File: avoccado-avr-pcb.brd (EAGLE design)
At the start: 17.8 x 40.3 mm, 30 parts, among them IC1 MCP1703CB, IC5 ATMEGA328P-20MU, Q1 #MHz, Q2 MOSFET-NCHANNEL2N7002PW, U1 ATMEGA328P, U2 MCP73831, X1 Micro USB

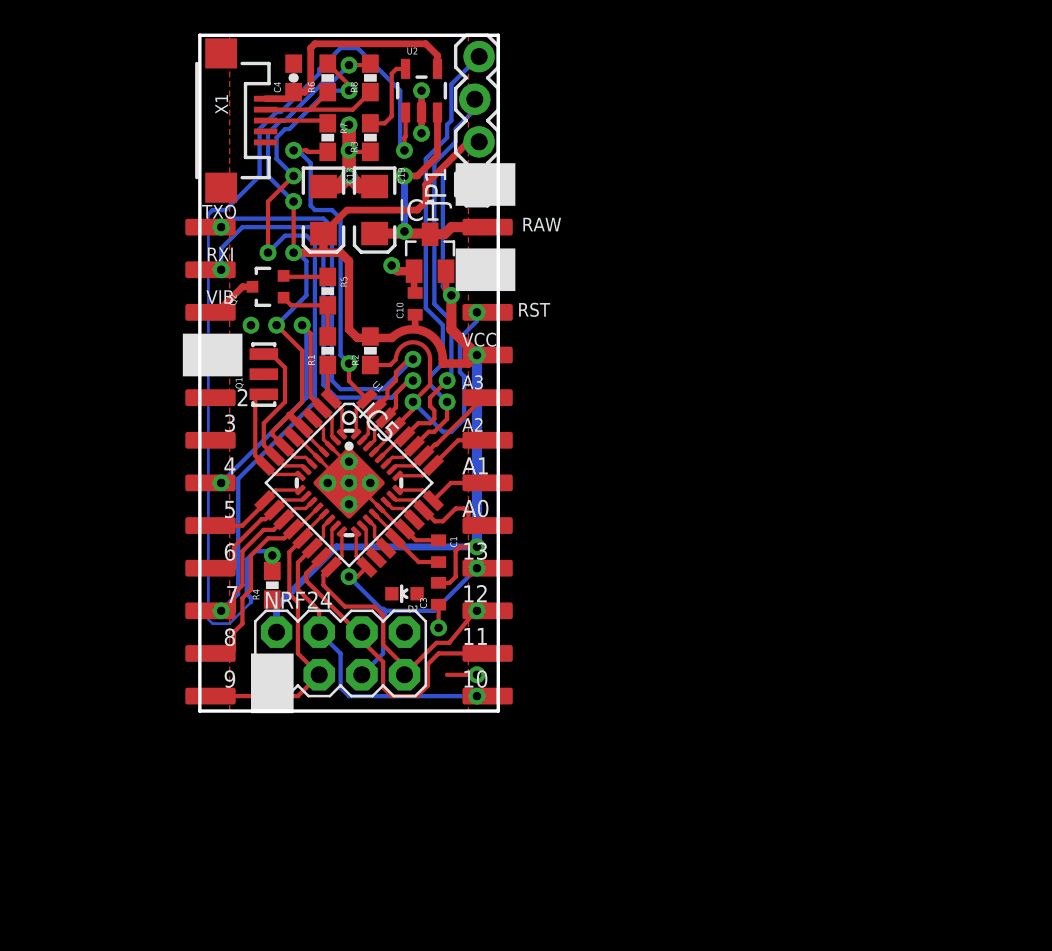
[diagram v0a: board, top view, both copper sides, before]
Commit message: reroute bottom header, reduce airwires
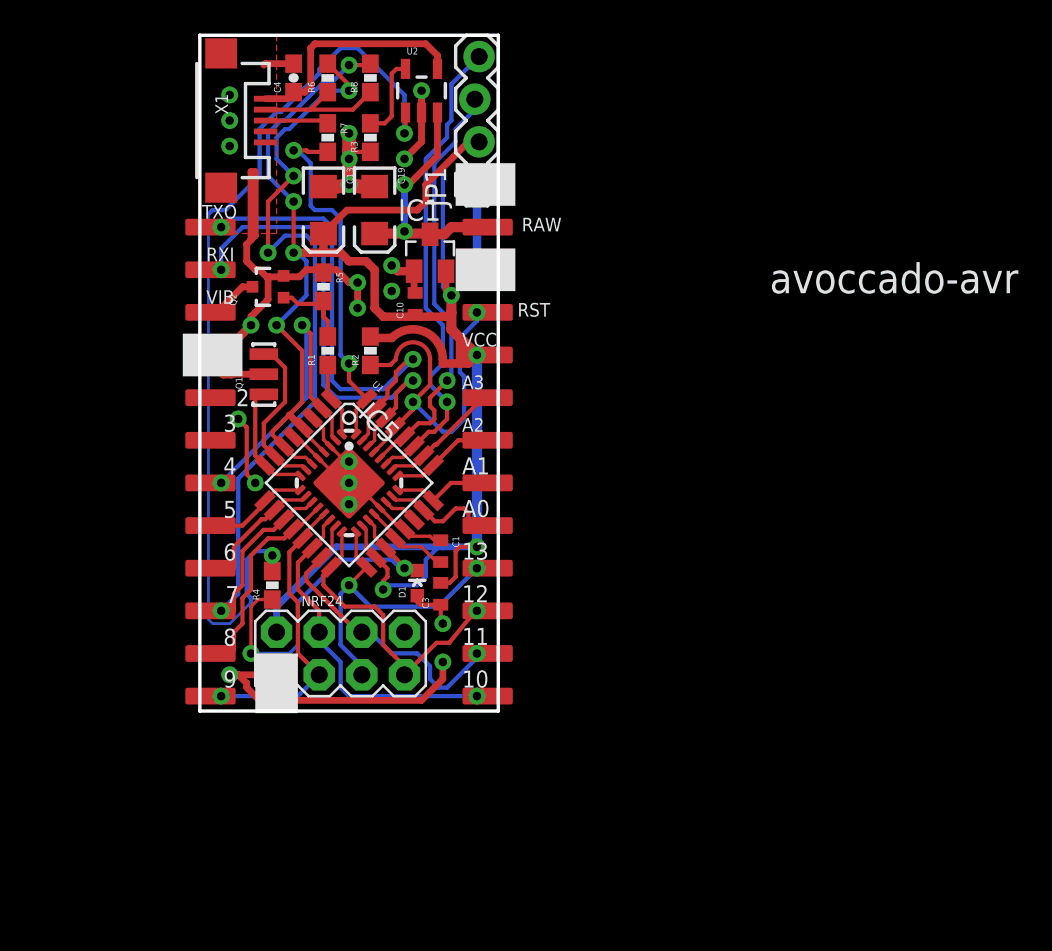
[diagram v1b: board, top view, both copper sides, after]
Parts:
- moved D1 0.99 mm to (21.8, 19.4), turned to 0 degrees
- moved R5 0.36 mm to (16.3, 37.1)
- moved C1 0.13 mm to (23.2, 21.3)
- moved C3 0.13 mm to (23.2, 18.8)
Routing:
- net GND: track 35.4 -> 99.2 mm, vias 16 -> 23
- net A6: track 2.13 -> 21.9 mm, vias 0 -> 2
- net 3V3: track 117.0 -> 127.6 mm, vias 7 -> 8
- net N$4: track 57.0 -> 55.0 mm
- net MOSI: track 20.7 -> 18.9 mm, vias 0 -> 1
- net SCK: track 18.2 -> 19.7 mm
- net BAT: track 16.9 -> 18.2 mm
- net D9: vias 0 -> 1

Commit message: minor corrections
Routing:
- net GND: track 99.2 -> 100.7 mm
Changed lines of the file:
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@@
 <layer number="14" name="Route14" color="1" fill="6" visible="no" active="no"/>
 <layer number="15" name="Route15" color="4" fill="6" visible="no" active="no"/>
-<layer number="16" name="Bottom" color="1" fill="1" visible="no" active="yes"/>
+<layer number="16" name="Bottom" color="1" fill="1" visible="yes" active="yes"/>
 <layer number="17" name="Pads" color="14" fill="1" visible="yes" active="yes"/>
 <layer number="18" name="Vias" color="14" fill="1" visible="yes" active="yes"/>
@@
 </layers>
 <board>
+<description>Avoccado-avr controller</description>
 <plain>
 <wire x1="8.89" y1="52.07" x2="8.89" y2="11.811" width="0.2032" layer="20"/>
@@
 <wire x1="17.78" y1="37.338" x2="17.018" y2="38.1" width="0.4064" layer="1"/>
 <wire x1="17.018" y1="38.1" x2="16.09" y2="38.1" width="0.4064" layer="1"/>
-<wire x1="18.288" y1="37.338" x2="18.288" y2="35.814" width="0.4064" layer="1"/>
 <via x="18.288" y="35.814" extent="1-16" drill="0.508" diameter="1.016"/>
 <via x="10.668" y="13.97" extent="1-16" drill="0.508" diameter="1.016"/>
@@
 <via x="11.176" y="29.21" extent="1-16" drill="0.508" diameter="1.016"/>
 <wire x1="11.684" y1="28.702" x2="11.176" y2="29.21" width="0.254" layer="1"/>
+<wire x1="20.32" y1="36.83" x2="20.32" y2="38.354" width="0.508" layer="1"/>
 <wire x1="10.16" y1="33.02" x2="9.525" y2="33.02" width="0" layer="19" extent="1-1"/>
 <wire x1="25.4" y1="38.1" x2="21.656" y2="38.016" width="0" layer="19" extent="1-1"/>
+<wire x1="18.288" y1="35.814" x2="18.288" y2="37.338" width="0.508" layer="1"/>
+<wire x1="18.288" y1="37.338" x2="25.4" y2="38.1" width="0" layer="19" extent="1-16"/>
 </signal>
 <signal name="AREF">
@@
 <contactref element="U1" pad="29"/>
 <contactref element="JP3" pad="3"/>
-<wire x1="26.035" y1="35.56" x2="25.4" y2="35.56" width="0.254" layer="1"/>
-<via x="25.4" y="35.56" extent="1-16" drill="0.508" diameter="1.016"/>
+<wire x1="26.035" y1="35.56" x2="25.019" y2="35.56" width="0.254" layer="1"/>
+<via x="25.019" y="35.56" extent="1-16" drill="0.508" diameter="1.016"/>
 <wire x1="23.368" y1="28.448" x2="23.876" y2="28.448" width="0.254" layer="16"/>
 <wire x1="23.876" y1="28.448" x2="24.638" y2="29.21" width="0.254" layer="16"/>
 <wire x1="24.638" y1="29.21" x2="24.638" y2="31.75" width="0.254" layer="16"/>
 <wire x1="24.638" y1="31.75" x2="24.384" y2="32.004" width="0.254" layer="16"/>
-<wire x1="24.384" y1="32.004" x2="24.384" y2="34.036" width="0.254" layer="16"/>
-<wire x1="24.384" y1="34.036" x2="25.4" y2="35.052" width="0.254" layer="16"/>
-<wire x1="25.4" y1="35.052" x2="25.4" y2="35.56" width="0.254" layer="16"/>
+<wire x1="24.384" y1="32.004" x2="24.384" y2="35.052" width="0.254" layer="16"/>
+<wire x1="24.384" y1="35.052" x2="25.019" y2="35.56" width="0.254" layer="16"/>
 <wire x1="20.53248125" y1="28.71816875" x2="21.59" y2="29.7756875" width="0.254" layer="1"/>
 <wire x1="21.59" y1="29.7756875" x2="21.59" y2="30.226" width="0.254" layer="1"/>

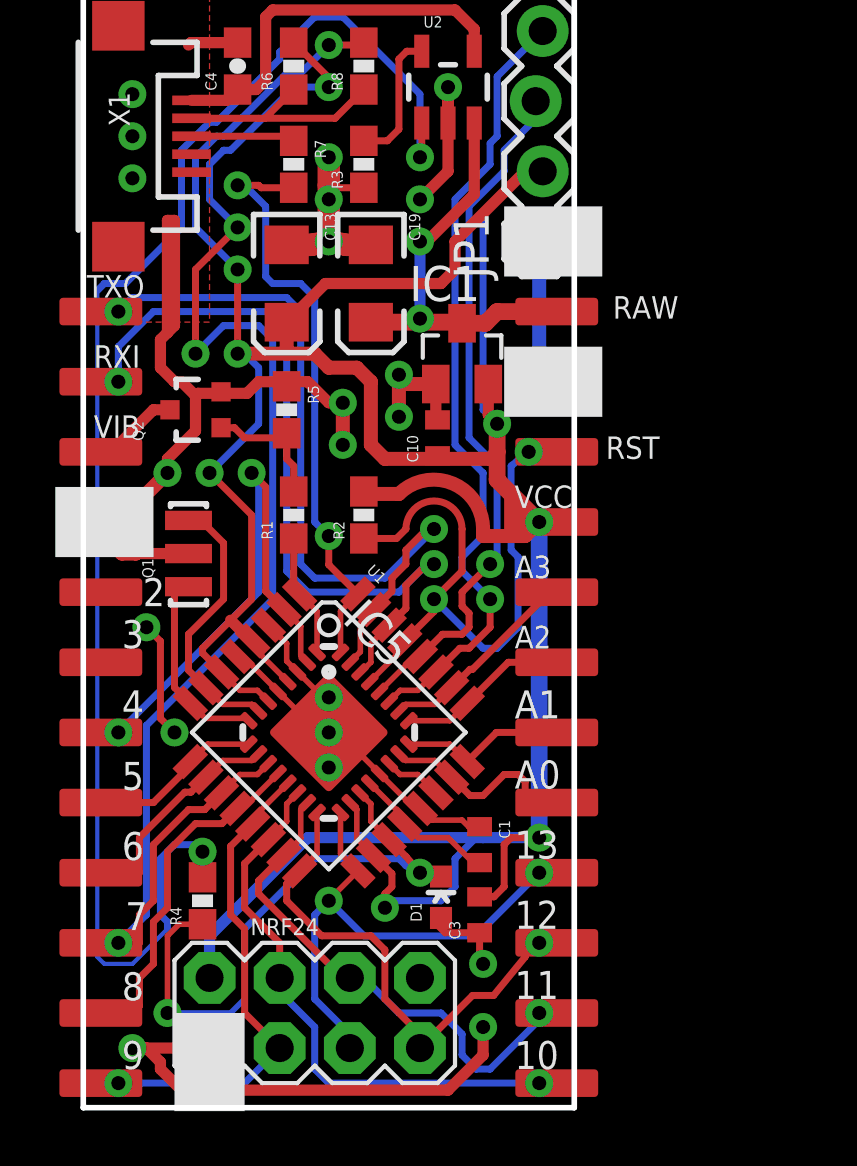
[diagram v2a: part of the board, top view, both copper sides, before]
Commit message: reroute GND layer, ditch pins 2&3
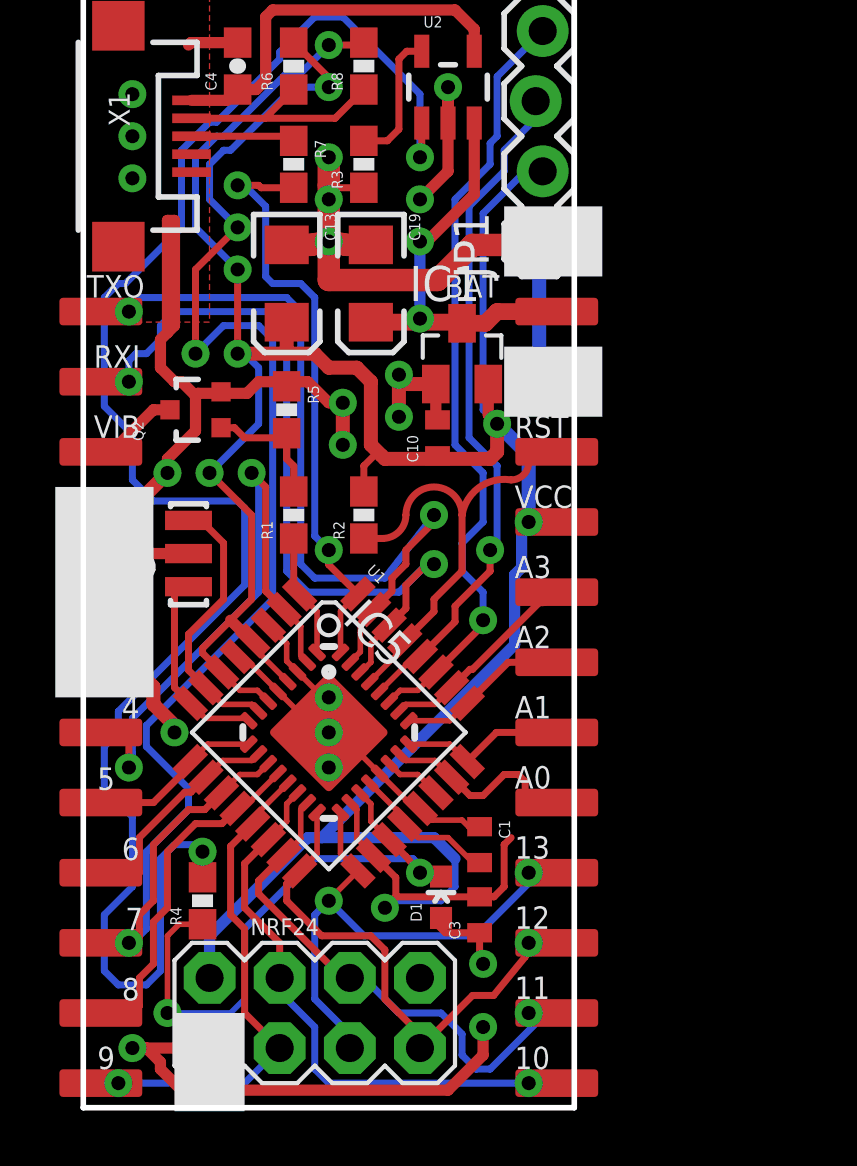
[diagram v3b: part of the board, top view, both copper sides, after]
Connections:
- net D2: no longer JP10.4
- net D3: no longer JP10.3
- net GND: now also JP10.3, JP10.4
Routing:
- net 3V3: track 127.6 -> 109.5 mm, vias 8 -> 7
- net N$4: track 55.0 -> 62.6 mm
- net RESET: track 22.5 -> 15.8 mm, vias 2 -> 0
- net GND: track 100.7 -> 107.1 mm, vias 23 -> 25
- net D4: track 19.9 -> 22.4 mm
- net D7: track 53.6 -> 54.8 mm
- net TXO: track 28.8 -> 29.6 mm
- net A5: track 25.3 -> 24.7 mm
- net MOSI: track 18.9 -> 19.5 mm
- net RXI: track 29.3 -> 28.8 mm
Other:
- board text added: "BAT"
- board text added: "GND"
- board text removed: "2"
- board text removed: "3"
- board text removed: "RAW"

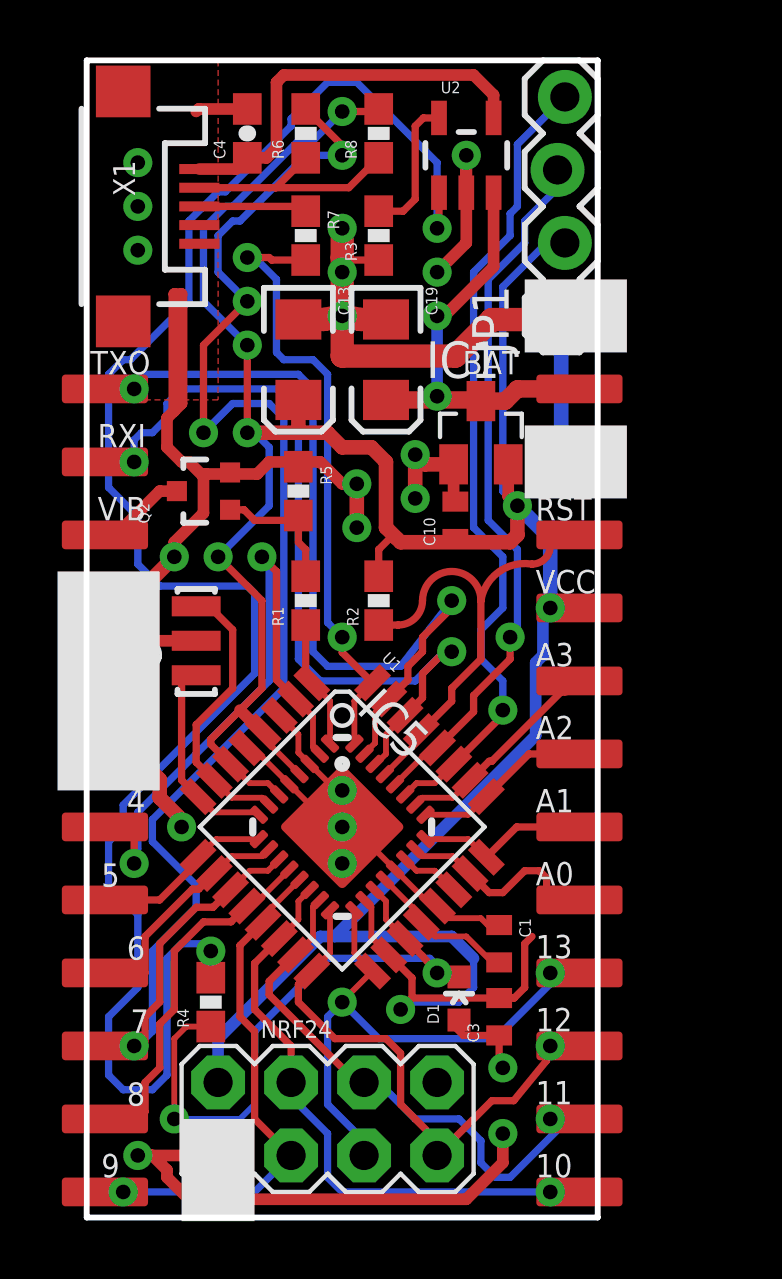
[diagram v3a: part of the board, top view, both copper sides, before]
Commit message: corrected DRC errors, mostly spacing
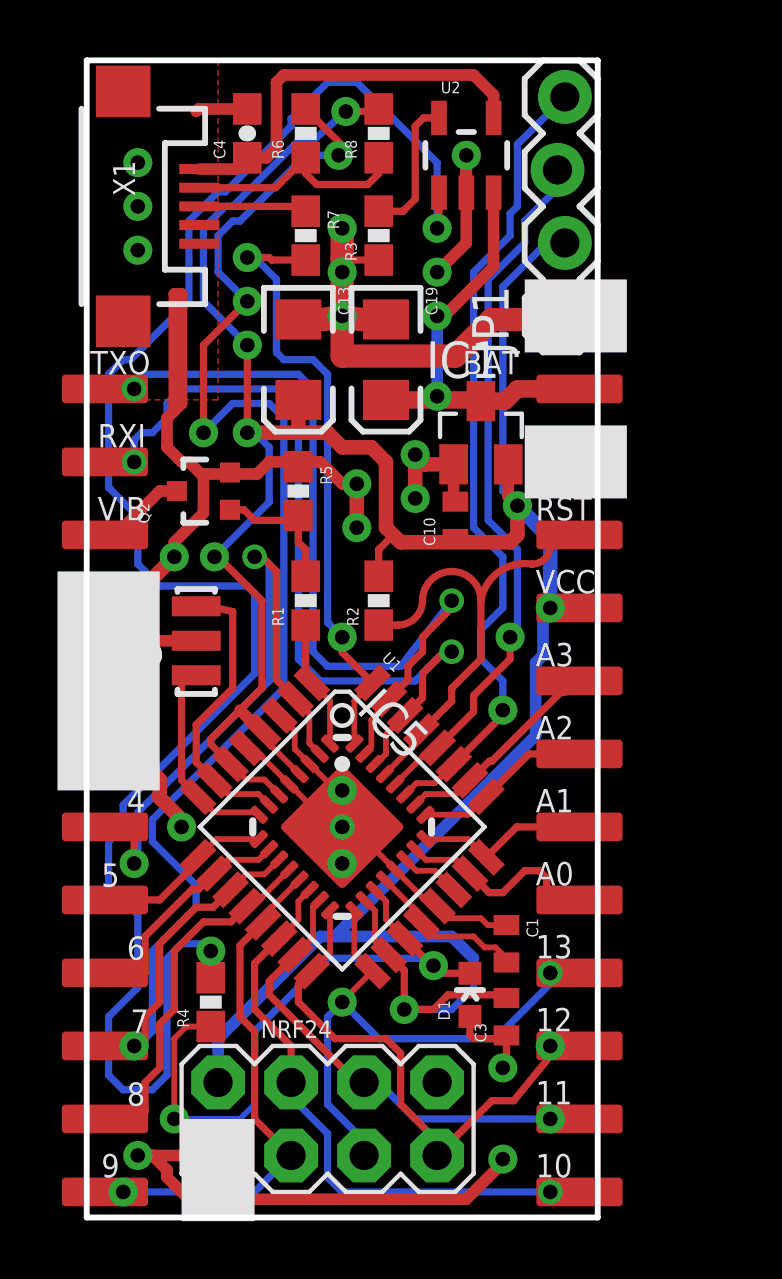
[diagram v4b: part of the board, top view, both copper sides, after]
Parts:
- moved D1 0.40 mm to (22.2, 19.6)
- moved C1 0.25 mm to (23.5, 21.3)
- moved C3 0.25 mm to (23.5, 18.8)
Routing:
- net GND: track 107.1 -> 100.8 mm, vias 25 -> 24
- net MOSI: track 19.5 -> 16.6 mm
- net 3V3: track 109.5 -> 107.1 mm
- net D4: track 22.4 -> 22.9 mm

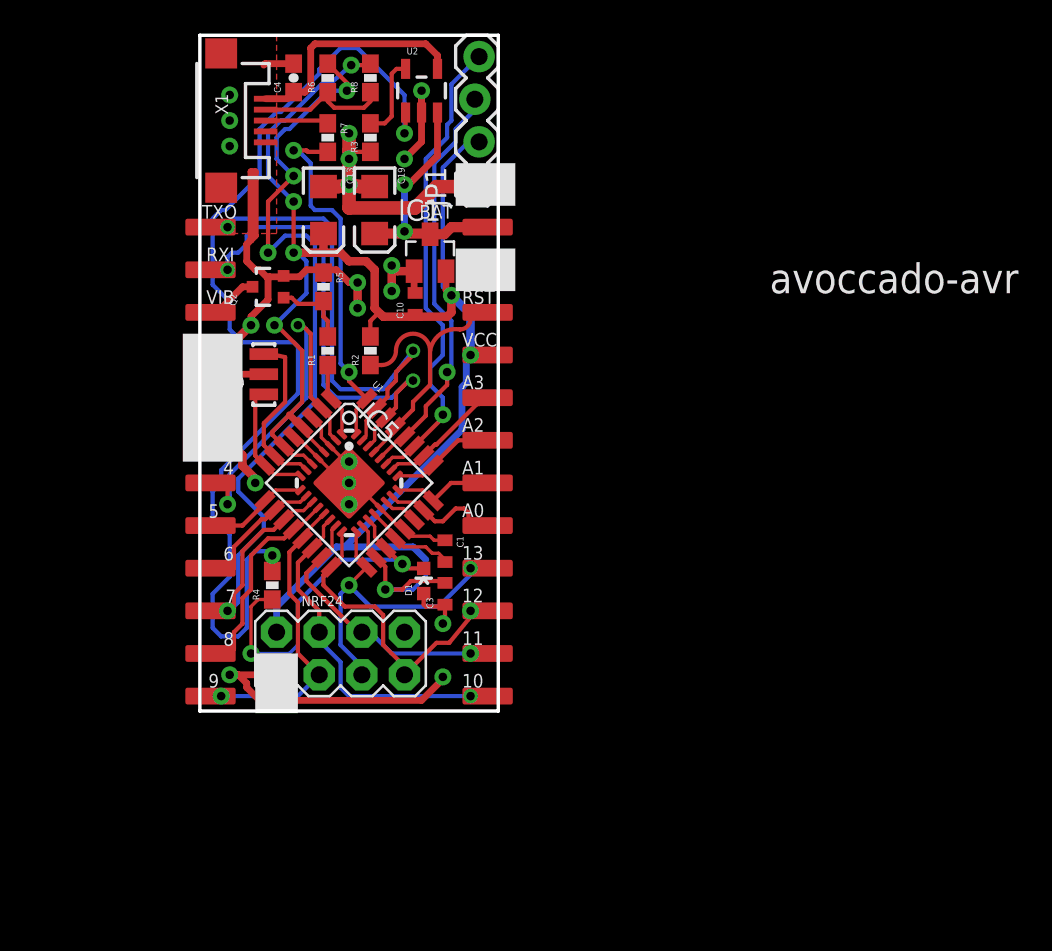
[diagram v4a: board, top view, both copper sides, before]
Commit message: increase board size to 19x42
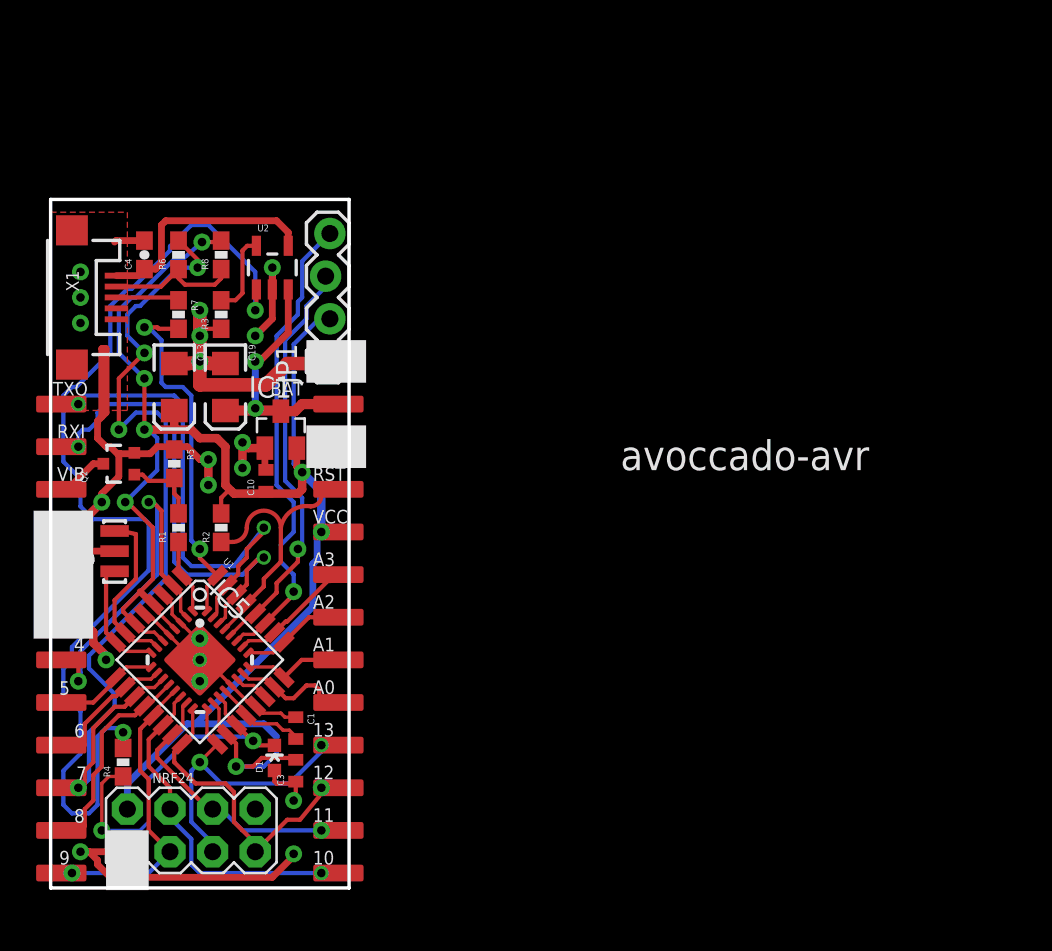
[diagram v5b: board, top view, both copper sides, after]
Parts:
- Q1: value #MHz -> 16MHz
- moved C4 13.8 mm to (5.59, 39.0)
- moved Q2 13.8 mm to (4.06, 26.5)
- moved R5 13.8 mm to (7.37, 26.5)
- moved R6 13.8 mm to (7.62, 39.0)
- moved R8 13.8 mm to (10.2, 39.0)
- moved U2 13.8 mm to (13.2, 38.2)
- moved X1 13.8 mm to (1.27, 36.4)
- moved C13 13.8 mm to (7.37, 31.1)
- moved D1 13.8 mm to (13.3, 9.02)
- moved IC1 13.8 mm to (13.7, 28.6)
- moved JP10 13.8 mm to (0.64, 16.1)
- moved JP5 13.8 mm to (17.1, 16.1)
- moved JP8 13.8 mm to (17.1, 5.97)
- moved JP9 13.8 mm to (0.64, 5.97)
- moved R1 13.8 mm to (7.62, 22.7)
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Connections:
- net BAT renamed VBAT
- removed net N$9: IC5.31
- net TXO: now also IC5.31
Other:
- board size 17.8 x 40.3 mm -> 17.8 x 41 mm
